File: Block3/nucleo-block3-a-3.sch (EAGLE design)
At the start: 51 parts, among them J4 MODJACK6P6C-MJ3245-66-0CONN_M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, J5 MODJACK6P6C-MJ3245-66-0CONN_M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, Q1 NPN-23, Q2 BSS84, U1 TC4428ACOA, U2 TC4428ACOA, U3 TC4428ACOA

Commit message: Adds loconet interrupt circuit. Links more things to the nucleo.
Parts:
- added C2, C3, C4: (no value), rcl:C-EUC0805
- added C5: 2.2nF, rcl:C-EUC0805
- added D3: (no value), diode:DIODE-MINIMELF
- added Q3: BSS84, eagleparts:BSS84
- added R22: 1M, rcl:R-EU_R0805
- added R23: 10k, rcl:R-EU_R0805
- added SJ1: (no value), eagleparts:SJ-C
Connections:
- removed net N$9: Q1.C, R5.1, R6.2
- new net LN-INT: G1.PC4, Q3.D
- new net LN-RX-S: D3.C, Q1.C, R5.1, R6.2
- new net LN-TX-P: G1.PC5, Q2.D, R7.1
- new net N$20: G1.PB14, SJ1.2
- new net N$22: C5.1, Q3.G, R22.2, R23.2
- net +5V: now also C2.2, C3.2, C4.2
- net GND: now also C2.1, C3.1, C4.1
- net LN-RX: now also G1.PA10, SJ1.1
- net LN-TX: now also C5.2, G1.PA9, Q3.S, R22.1
- net N$10: now also D3.A, R23.1; no longer Q2.D, R7.1
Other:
- note added: "Generates LN interrupt when TX=high and RX=low for 20 usec."
- moved on the sheet: R10

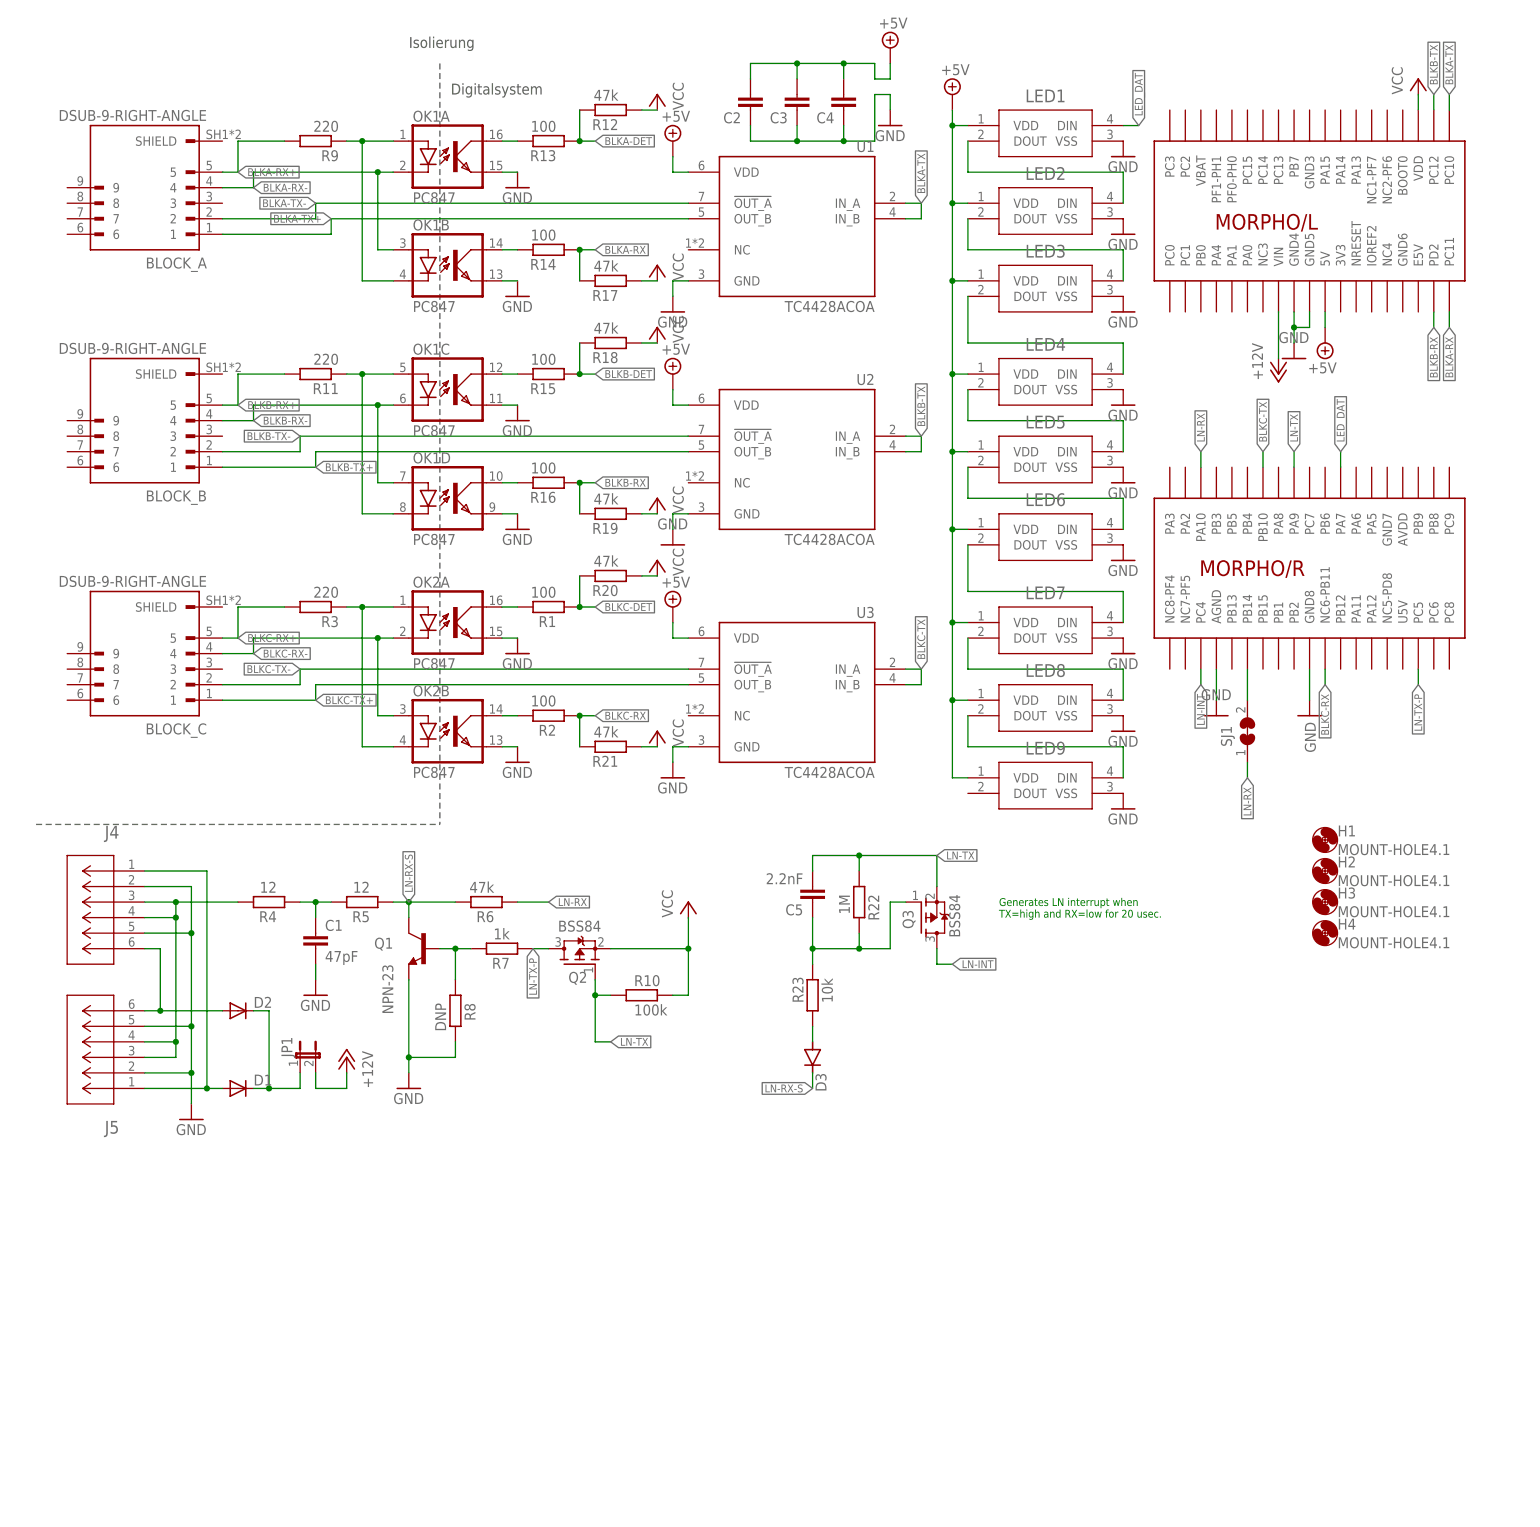
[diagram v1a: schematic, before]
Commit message: Adds analog read-in buttons.
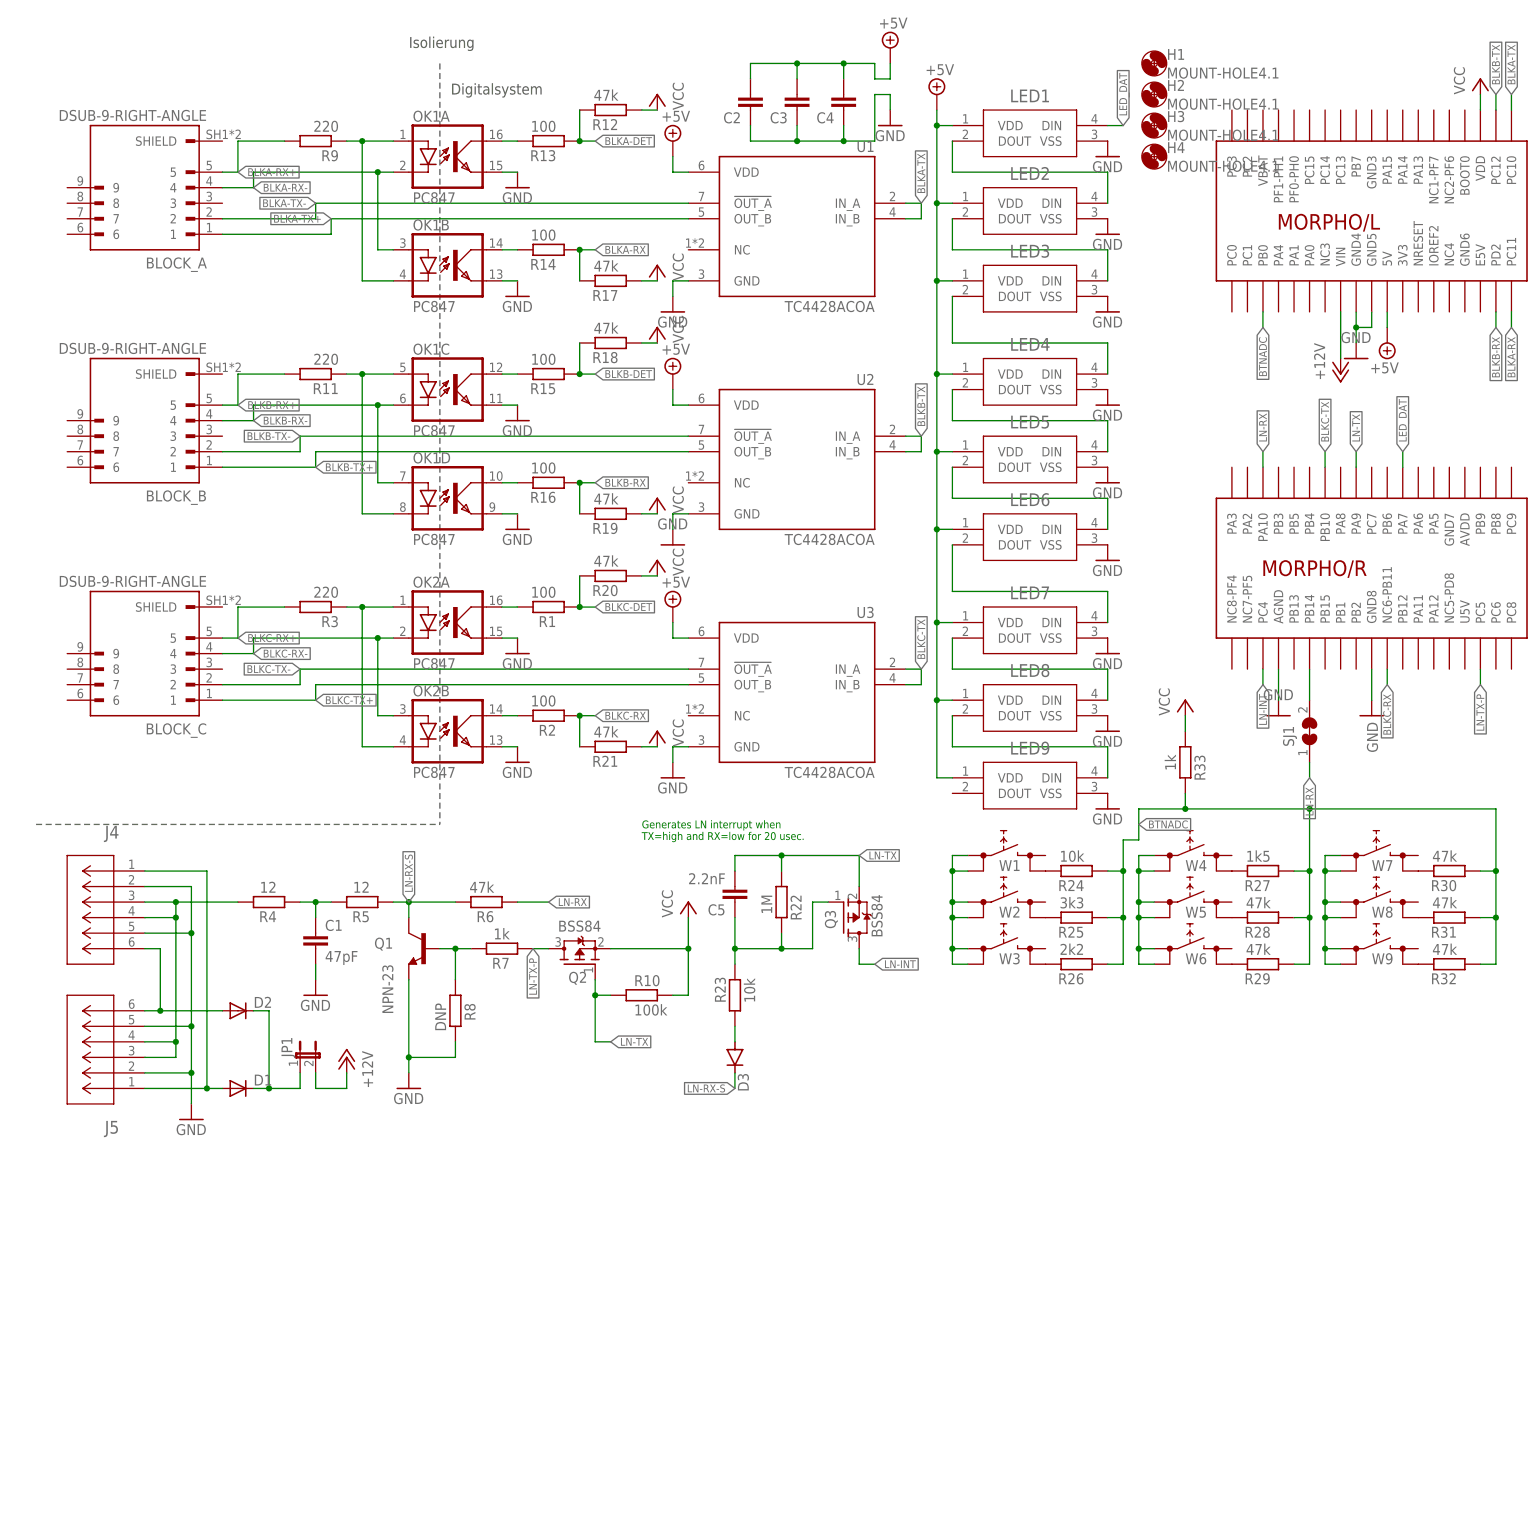
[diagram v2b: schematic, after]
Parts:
- added R24: 10k, rcl:R-EU_R0603
- added R25: 3k3, rcl:R-EU_R0603
- added R26: 2k2, rcl:R-EU_R0603
- added R27: 1k5, rcl:R-EU_R0603
- added R28, R29, R30, R31, R32: 47k, rcl:R-EU_R0603
- added R33: 1k, rcl:R-EU_R0805
- added W1, W2, W3, W4, W5, W6, W7, W8, W9: W1, g-e2e-training:TACTSW-6X6S
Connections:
- new net BTNADC: G1.PB0, R24.1, R25.1, R26.1, R27.1, R28.1, R29.1, R30.1, R31.1, R32.1, R33.2
- new net N$21: R25.2, W2.2.2
- new net N$23: R26.2, W3.2.2
- new net N$24: W1.1.1, W1.1.2, W2.1.1, W2.1.2, W3.1.1, W3.1.2
- new net N$26: R27.2, W4.2.2
- new net N$27: R28.2, W5.2.2
- new net N$28: R29.2, W6.2.2
- new net N$29: W4.1.1, W4.1.2, W5.1.1, W5.1.2, W6.1.1, W6.1.2
- new net N$32: R30.2, W7.2.2
- new net N$33: R31.2, W8.2.2
- new net N$34: R32.2, W9.2.2
- new net N$36: W7.1.1, W7.1.2, W8.1.1, W8.1.2, W9.1.1, W9.1.2
- new net N$9: R24.2, W1.2.2
- net VCC: now also R33.1
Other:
- moved on the sheet: C5, D3, H1, H2, H3, H4, LED1, LED2, LED3, LED4, LED5, LED6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

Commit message: Adds routing of the loconet input voltage to an NC pin to drive the 5V switcher. Adds a comparator based loconet input voltage decoder. Finishes the button grid.
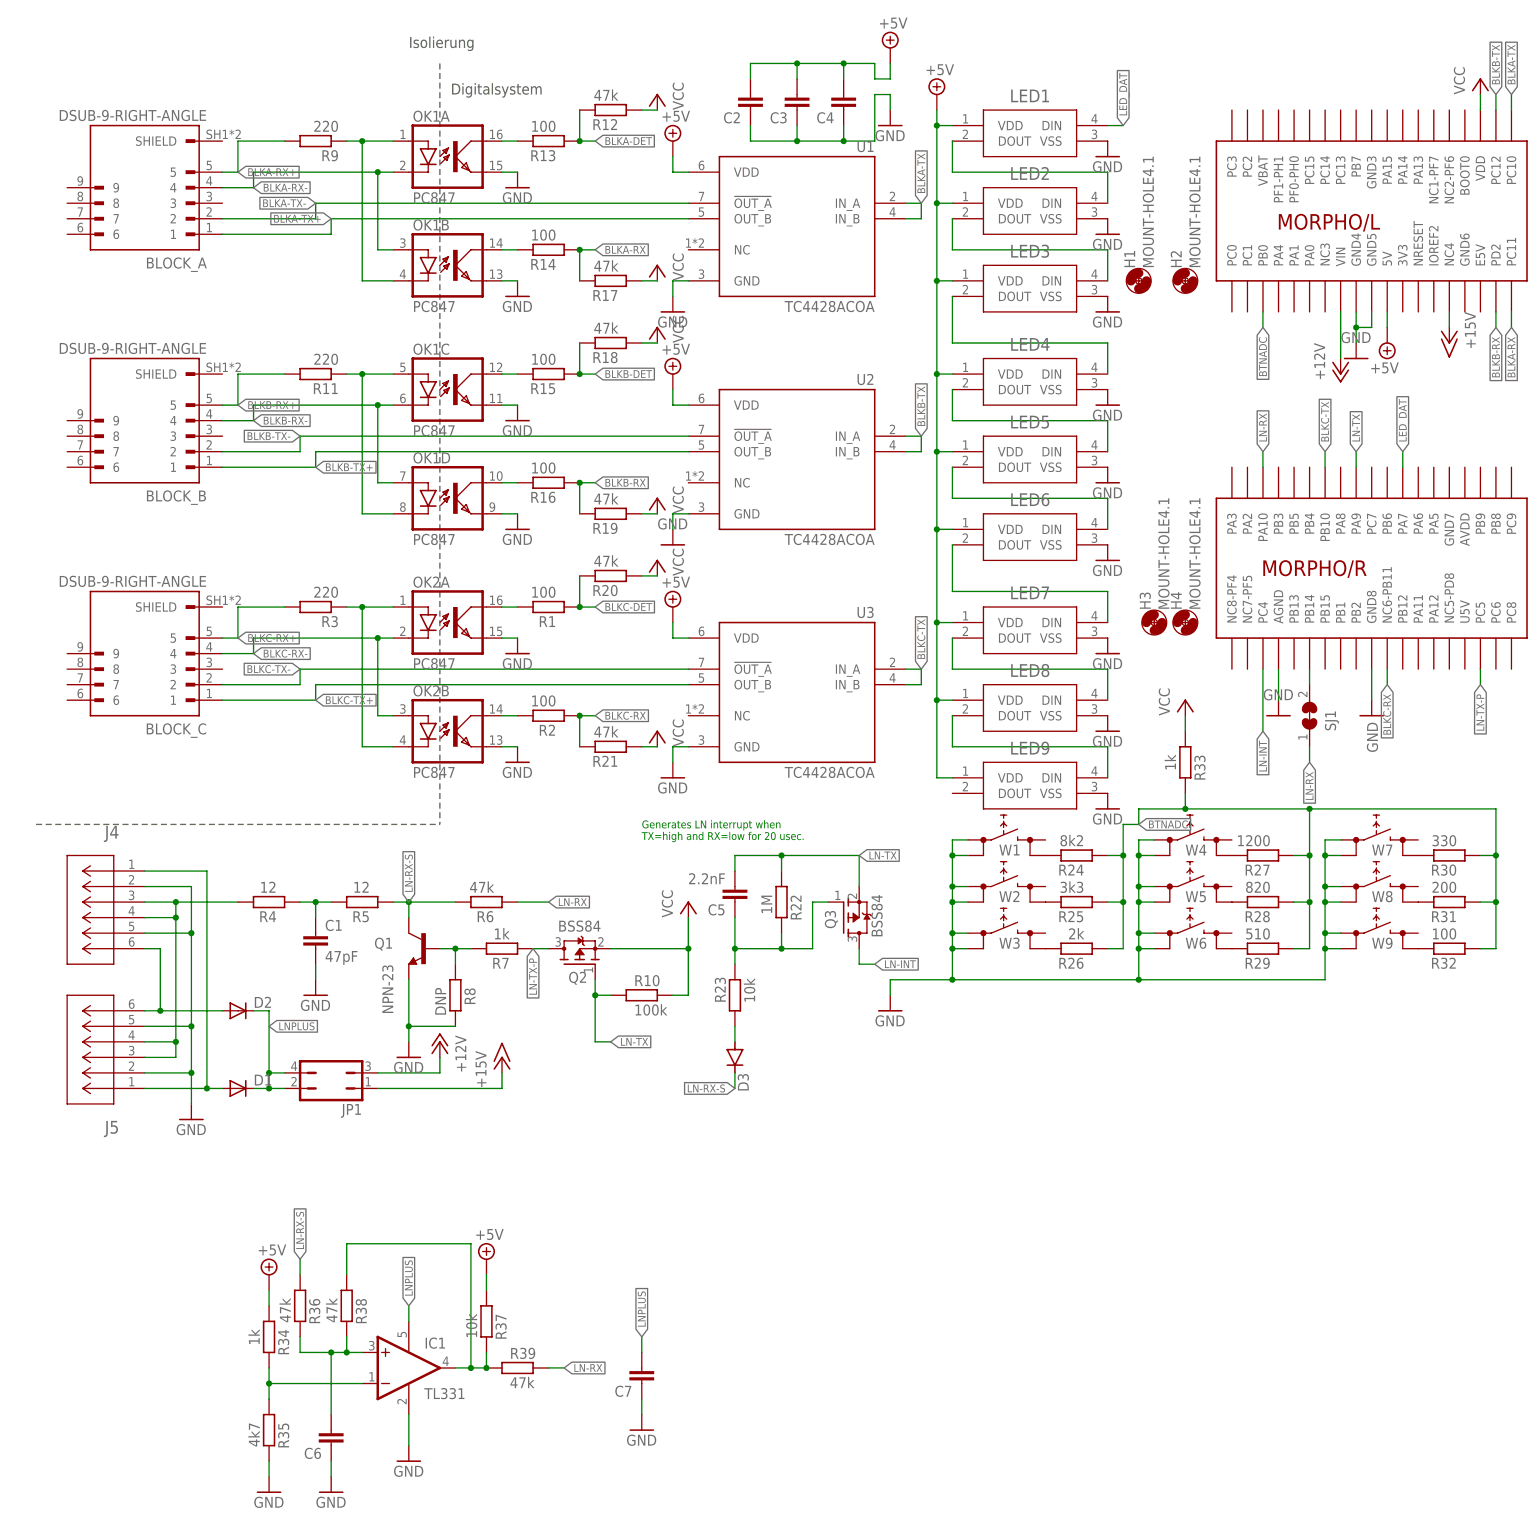
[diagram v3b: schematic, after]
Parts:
- added C6, C7: (no value), rcl:C-EUC0805
- added IC1: TL331, linear:TL331
- added R34: 1k, rcl:R-EU_R0805
- added R35: 4k7, rcl:R-EU_R0805
- added R36, R38, R39: 47k, rcl:R-EU_R0805
- added R37: 10k, rcl:R-EU_R0805
- JP1: device jumper:JP1E -> jumper:JP2Q
- R24: value 10k -> 8k2
- R26: value 2k2 -> 2k
- R27: value 1k5 -> 1200
- R28: value 47k -> 820
- R29: value 47k -> 510
- R30: value 47k -> 330
- R31: value 47k -> 200
- R32: value 47k -> 100
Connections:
- removed net N$29: W4.1.1, W4.1.2, W5.1.1, W5.1.2, W6.1.1, W6.1.2
- removed net N$36: W7.1.1, W7.1.2, W8.1.1, W8.1.2, W9.1.1, W9.1.2
- new net +15V: G1.NC4, JP1.1
- new net LNPLUS: C7.2, D1.C, D2.C, IC1.V+, JP1.2, JP1.4
- new net N$25: IC1.OUT, R37.2, R38.1, R39.1
- net +12V: now also JP1.3; no longer JP1.2
- net +5V: now also R34.1, R37.1
- net GND: now also C6.1, C7.1, IC1.GND, R35.2, W1.1.1, W1.1.2, W2.1.1, W2.1.2, W3.1.1, W3.1.2, W4.1.1, W4.1.2, W5.1.1, W5.1.2, W6.1.1, W6.1.2, W7.1.1, W7.1.2, W8.1.1, W8.1.2, W9.1.1, W9.1.2
- net LN-RX: now also R39.2
- net LN-RX-S: now also R36.1
- net N$24: now also C6.2, IC1.+IN, R36.2, R38.2; no longer W1.1.1, W1.1.2, W2.1.1, W2.1.2, W3.1.1, W3.1.2
- net N$8: now also IC1.-IN, R34.2, R35.1; no longer D1.C, D2.C, JP1.1
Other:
- moved on the sheet: H1, H2, H3, H4, R24, R25, R26, R27, R28, R29, R30, R31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
